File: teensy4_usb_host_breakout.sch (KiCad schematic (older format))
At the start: 11 parts, among them J1 Conn_01x06, J2 USB_A, U1 TPD3S014

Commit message: Update footprintso
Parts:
- C1: footprint Capacitor_SMD:C_0603_1608Metric_Pad1.05x0.95mm_HandSolder -> Capacitor_SMD:C_0805_2012Metric_Pad1.15x1.40mm_HandSolder
- C2: footprint Capacitor_Tantalum_SMD:CP_EIA-1608-08_AVX-J_Pad1.25x1.05mm_HandSolder -> Capacitor_SMD:C_1206_3216Metric_Pad1.42x1.75mm_HandSolder
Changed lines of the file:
@@
 F 0 "C2" H 5765 4396 50  0000 L CNN
 F 1 "100u" H 5765 4305 50  0000 L CNN
-F 2 "Capacitor_Tantalum_SMD:CP_EIA-1608-08_AVX-J_Pad1.25x1.05mm_HandSolder" H 5650 4350 50  0001 C CNN
+F 2 "Capacitor_SMD:C_1206_3216Metric_Pad1.42x1.75mm_HandSolder" H 5650 4350 50  0001 C CNN
 F 3 "~" H 5650 4350 50  0001 C CNN
 	1    5650 4350
@@
 F 0 "C1" H 5065 4396 50  0000 L CNN
 F 1 "2u2" H 5065 4305 50  0000 L CNN
-F 2 "Capacitor_SMD:C_0603_1608Metric_Pad1.05x0.95mm_HandSolder" H 4950 4350 50  0001 C CNN
+F 2 "Capacitor_SMD:C_0805_2012Metric_Pad1.15x1.40mm_HandSolder" H 4950 4350 50  0001 C CNN
 F 3 "~" H 4950 4350 50  0001 C CNN
 	1    4950 4350

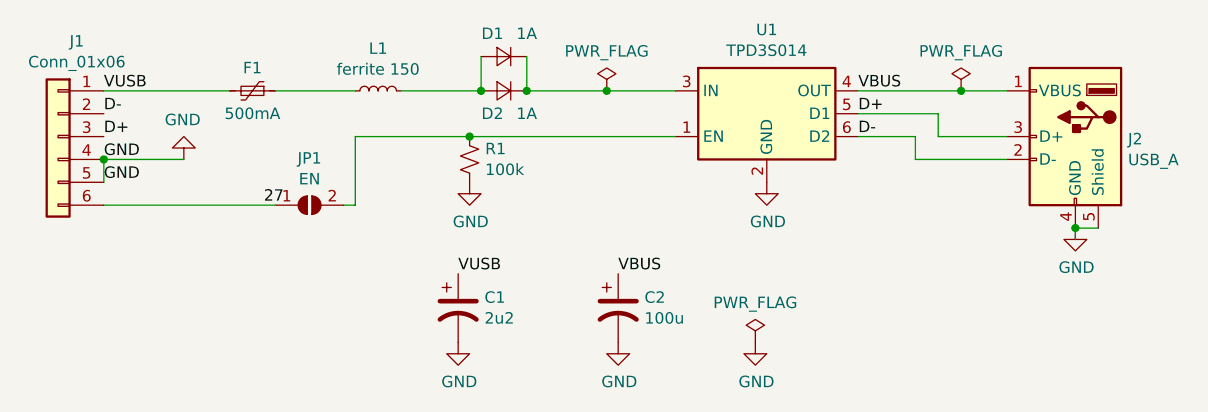
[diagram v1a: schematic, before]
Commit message: Updated with Digikey part numbers. Removed diodes as TPD3S014DBVR provides reverse voltage protection
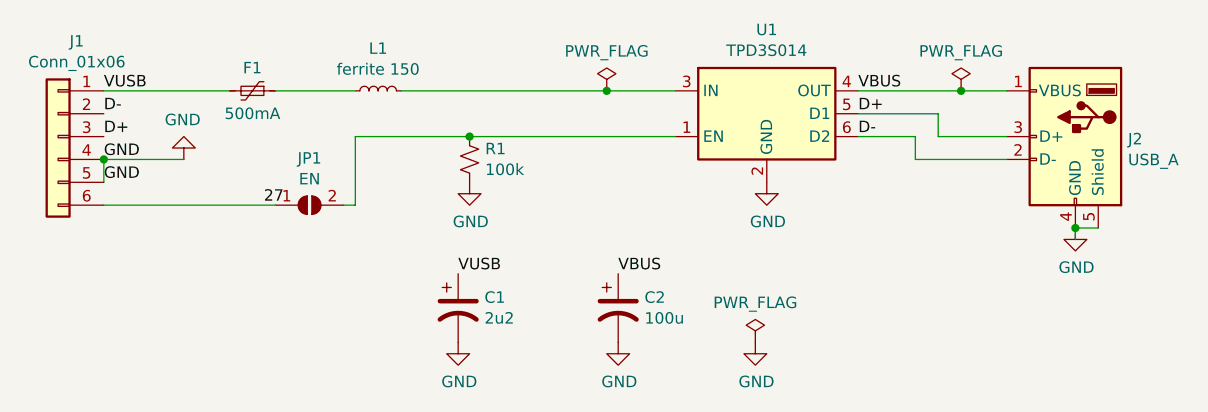
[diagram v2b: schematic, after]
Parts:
- removed D1, D2: 1A, Diode_SMD:D_0805_2012Metric_Pad1.15x1.40mm_HandSolder, symbol Device:D_Small
- C1: Digikey (none) -> 1276-1188-1-ND
- C2: Digikey (none) -> ‎478-12404-1-ND‎
- F1: Digikey (none) -> 507-1813-1-ND
- J2: Digikey (none) -> 732-11179-1-ND
- L1: Digikey (none) -> ‎490-1038-1-ND‎
- R1: Digikey (none) -> 311-100KCRCT-ND
- U1: Digikey (none) -> 296-38835-1-ND
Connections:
- wire segments 24 -> 21
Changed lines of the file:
@@
 F 2 "USB_A_Receptacle_SMD_Wuerth_629104190121:USB_A_Receptacle_SMD_Wuerth_629104190121" H 7800 3550 50  0001 C CNN
 F 3 " ~" H 7800 3550 50  0001 C CNN
+F 4 "732-11179-1-ND" H 7650 3600 50  0001 C CNN "Digikey"
 	1    7650 3600
 	-1   0    0    -1
@@
 F 2 "Package_TO_SOT_SMD:SOT-23-6" H 6300 3850 50  0001 C CNN
 F 3 "http://www.ti.com/lit/ds/symlink/tpd3s014.pdf" H 6100 3750 50  0001 C CNN
+F 4 "296-38835-1-ND" H 6300 3500 50  0001 C CNN "Digikey"
 	1    6300 3500
 	1    0    0    -1
@@
 F 2 "Resistor_SMD:R_0805_2012Metric_Pad1.15x1.40mm_HandSolder" H 5000 3700 50  0001 C CNN
 F 3 "~" H 5000 3700 50  0001 C CNN
+F 4 "311-100KCRCT-ND" H 5000 3700 50  0001 C CNN "Digikey"
 	1    5000 3700
 	1    0    0    -1
@@
 F 2 "Capacitor_SMD:C_1206_3216Metric_Pad1.42x1.75mm_HandSolder" H 5650 4350 50  0001 C CNN
 F 3 "~" H 5650 4350 50  0001 C CNN
+F 4 "‎478-12404-1-ND‎" H 5650 4350 50  0001 C CNN "Digikey"
 	1    5650 4350
 	1    0    0    -1
@@
 F 2 "Capacitor_SMD:C_0805_2012Metric_Pad1.15x1.40mm_HandSolder" H 4950 4350 50  0001 C CNN
 F 3 "~" H 4950 4350 50  0001 C CNN
+F 4 "1276-1188-1-ND" H 4950 4350 50  0001 C CNN "Digikey"
 	1    4950 4350
 	1    0    0    -1
@@
 F 2 "Inductor_SMD:L_0805_2012Metric_Pad1.15x1.40mm_HandSolder" H 4100 3200 50  0001 L CNN
 F 3 "~" H 4050 3400 50  0001 C CNN
+F 4 "507-1813-1-ND" V 4050 3400 50  0001 C CNN "Digikey"
 	1    4050 3400
 	0    1    1    0
@@
 Wire Wire Line
 	3400 3400 3950 3400
-$Comp
-L Device:D_Small D2
-U 1 1 5D862829
-P 5150 3400
-F 0 "D2" H 5200 3500 50  0000 C CNN
-F 1 "1A" H 5050 3500 50  0000 C CNN
-F 2 "Diode_SMD:D_0805_2012Metric_Pad1.15x1.40mm_HandSolder" V 5150 3400 50  0001 C CNN
-F 3 "~" V 5150 3400 50  0001 C CNN
-	1    5150 3400
-	-1   0    0    1
-$EndComp
-$Comp
-L Device:D_Small D1
-U 1 1 5D863E89
-P 5150 3250
-F 0 "D1" H 5200 3150 50  0000 C CNN
-F 1 "1A" H 5050 3150 50  0000 C CNN
-F 2 "Diode_SMD:D_0805_2012Metric_Pad1.15x1.40mm_HandSolder" V 5150 3250 50  0001 C CNN
-F 3 "~" V 5150 3250 50  0001 C CNN
-	1    5150 3250
-	-1   0    0    1
-$EndComp
-Wire Wire Line
-	4700 3400 5050 3400
 $Comp
 L Device:L_Small L1
@@
 F 2 "Inductor_SMD:L_0805_2012Metric_Pad1.15x1.40mm_HandSolder" H 4600 3400 50  0001 C CNN
 F 3 "~" H 4600 3400 50  0001 C CNN
+F 4 "‎490-1038-1-ND‎" V 4600 3400 50  0001 C CNN "Digikey"
 	1    4600 3400
 	0    -1   -1   0
@@
 	4150 3400 4500 3400
 Wire Wire Line
-	5050 3250 5050 3400
-Connection ~ 5050 3400
-Wire Wire Line
-	5250 3250 5250 3400
-Wire Wire Line
 	5900 3400 5600 3400
-Connection ~ 5250 3400
 $Comp
 L Jumper:SolderJumper_2_Open JP1
@@
 	1    0    0    -1
 $EndComp
+Wire Wire Line
+	4700 3400 5600 3400
 Connection ~ 5600 3400
-Wire Wire Line
-	5600 3400 5250 3400
 $EndSCHEMATC

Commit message: Updated for jumper for enable (always on vs 27). Also updated docs
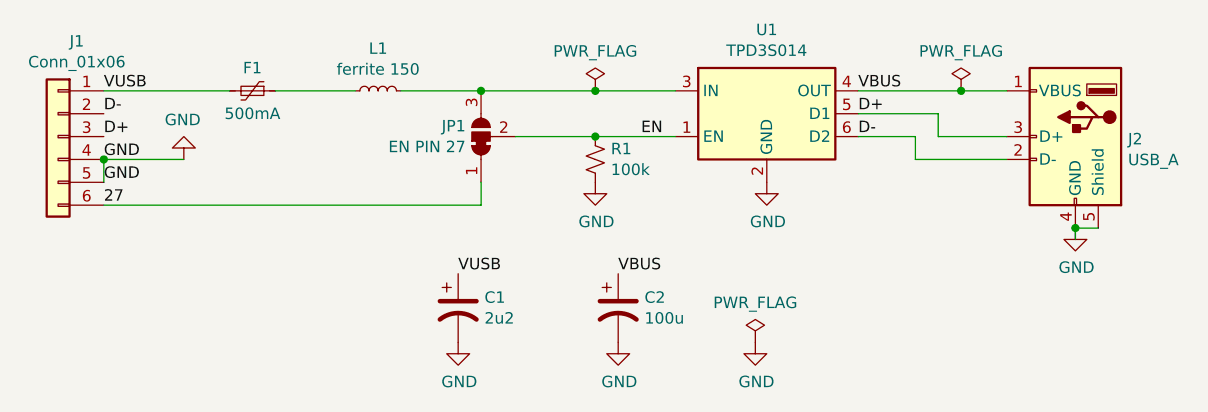
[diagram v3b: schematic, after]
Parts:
- removed JP1: EN, Jumper:SolderJumper-2_P1.3mm_Open_RoundedPad1.0x1.5mm, symbol Jumper:SolderJumper_2_Open
- added JP1: EN PIN 27, Jumper:SolderJumper-3_P1.3mm_Bridged12_RoundedPad1.0x1.5mm, symbol Jumper:SolderJumper_3_Bridged12
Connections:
- net labels added: EN
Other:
- moved on the sheet: R1
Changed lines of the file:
@@
 Text Label 3400 3800 0    50   ~ 0
 GND
-Text Label 4100 3900 0    50   ~ 0
+Text Label 3400 3900 0    50   ~ 0
 27
 $Comp
@@
 	1    0    0    -1
 $EndComp
-$Comp
-L Device:R_Small_US R1
-U 1 1 5D85600F
-P 5000 3700
-F 0 "R1" H 5068 3746 50  0000 L CNN
-F 1 "100k" H 5068 3655 50  0000 L CNN
-F 2 "Resistor_SMD:R_0805_2012Metric_Pad1.15x1.40mm_HandSolder" H 5000 3700 50  0001 C CNN
-F 3 "~" H 5000 3700 50  0001 C CNN
-F 4 "311-100KCRCT-ND" H 5000 3700 50  0001 C CNN "Digikey"
-	1    5000 3700
-	1    0    0    -1
-$EndComp
-Wire Wire Line
-	5000 3600 5900 3600
 Wire Wire Line
 	3400 3700 3400 3800
-$Comp
-L power:GND #PWR0101
-U 1 1 5D857668
-P 5000 3800
-F 0 "#PWR0101" H 5000 3550 50  0001 C CNN
-F 1 "GND" H 5005 3627 50  0000 C CNN
-F 2 "" H 5000 3800 50  0001 C CNN
-F 3 "" H 5000 3800 50  0001 C CNN
-	1    5000 3800
-	1    0    0    -1
-$EndComp
 $Comp
 L power:GND #PWR0102
@@
 	3400 3700 3750 3700
 Connection ~ 3400 3700
-Wire Wire Line
-	3400 3900 4150 3900
-Wire Wire Line
-	4500 3900 4500 3600
-Wire Wire Line
-	4500 3600 5000 3600
-Connection ~ 5000 3600
 Wire Wire Line
 	6950 3600 6950 3700
@@
 	4150 3400 4500 3400
 Wire Wire Line
-	5900 3400 5600 3400
-$Comp
-L Jumper:SolderJumper_2_Open JP1
-U 1 1 5D870030
-P 4300 3900
-F 0 "JP1" H 4300 4105 50  0000 C CNN
-F 1 "EN" H 4300 4014 50  0000 C CNN
-F 2 "Jumper:SolderJumper-2_P1.3mm_Open_RoundedPad1.0x1.5mm" H 4300 3900 50  0001 C CNN
-F 3 "~" H 4300 3900 50  0001 C CNN
-	1    4300 3900
-	1    0    0    -1
-$EndComp
-Wire Wire Line
-	4450 3900 4500 3900
+	5900 3400 5550 3400
+Wire Wire Line
+	5200 3600 5550 3600
 Text Label 6700 3500 0    50   ~ 0
 D+
@@
 L power:PWR_FLAG #FLG0103
 U 1 1 5D8737A7
-P 5600 3400
-F 0 "#FLG0103" H 5600 3475 50  0001 C CNN
-F 1 "PWR_FLAG" H 5600 3573 50  0000 C CNN
-F 2 "" H 5600 3400 50  0001 C CNN
-F 3 "~" H 5600 3400 50  0001 C CNN
-	1    5600 3400
-	1    0    0    -1
-$EndComp
-Wire Wire Line
-	4700 3400 5600 3400
-Connection ~ 5600 3400
+P 5550 3400
+F 0 "#FLG0103" H 5550 3475 50  0001 C CNN
+F 1 "PWR_FLAG" H 5550 3573 50  0000 C CNN
+F 2 "" H 5550 3400 50  0001 C CNN
+F 3 "~" H 5550 3400 50  0001 C CNN
+	1    5550 3400
+	1    0    0    -1
+$EndComp
+Connection ~ 5550 3400
+Connection ~ 5550 3600
+Wire Wire Line
+	5550 3600 5900 3600
+$Comp
+L power:GND #PWR0101
+U 1 1 5D857668
+P 5550 3800
+F 0 "#PWR0101" H 5550 3550 50  0001 C CNN
+F 1 "GND" H 5555 3627 50  0000 C CNN
+F 2 "" H 5550 3800 50  0001 C CNN
+F 3 "" H 5550 3800 50  0001 C CNN
+	1    5550 3800
+	1    0    0    -1
+$EndComp
+$Comp
+L Device:R_Small_US R1
+U 1 1 5D85600F
+P 5550 3700
+F 0 "R1" H 5618 3746 50  0000 L CNN
+F 1 "100k" H 5618 3655 50  0000 L CNN
+F 2 "Resistor_SMD:R_0805_2012Metric_Pad1.15x1.40mm_HandSolder" H 5550 3700 50  0001 C CNN
+F 3 "~" H 5550 3700 50  0001 C CNN
+F 4 "311-100KCRCT-ND" H 5550 3700 50  0001 C CNN "Digikey"
+	1    5550 3700
+	1    0    0    -1
+$EndComp
+$Comp
+L Jumper:SolderJumper_3_Bridged12 JP1
+U 1 1 5D98F81D
+P 5050 3600
+F 0 "JP1" V 5096 3667 50  0000 L CNN
+F 1 "EN PIN 27" V 5005 3667 50  0000 L CNN
+F 2 "Jumper:SolderJumper-3_P1.3mm_Bridged12_RoundedPad1.0x1.5mm" H 5050 3600 50  0001 C CNN
+F 3 "~" H 5050 3600 50  0001 C CNN
+	1    5050 3600
+	0    -1   -1   0
+$EndComp
+Text Label 5750 3600 0    50   ~ 0
+EN
+Wire Wire Line
+	5050 3900 5050 3800
+Wire Wire Line
+	5050 3400 5550 3400
+Wire Wire Line
+	4700 3400 5050 3400
+Connection ~ 5050 3400
+Wire Wire Line
+	3400 3900 5050 3900
 $EndSCHEMATC
